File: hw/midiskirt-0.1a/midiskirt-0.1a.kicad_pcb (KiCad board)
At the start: 2 copper layers, 13 parts, among them J1 DIN-5, J2 DIN-5, J3 DIN-5, U1 MC6850, U2 C64-Exp-Port, U3 74LS30, U4 4049, U5 6N137

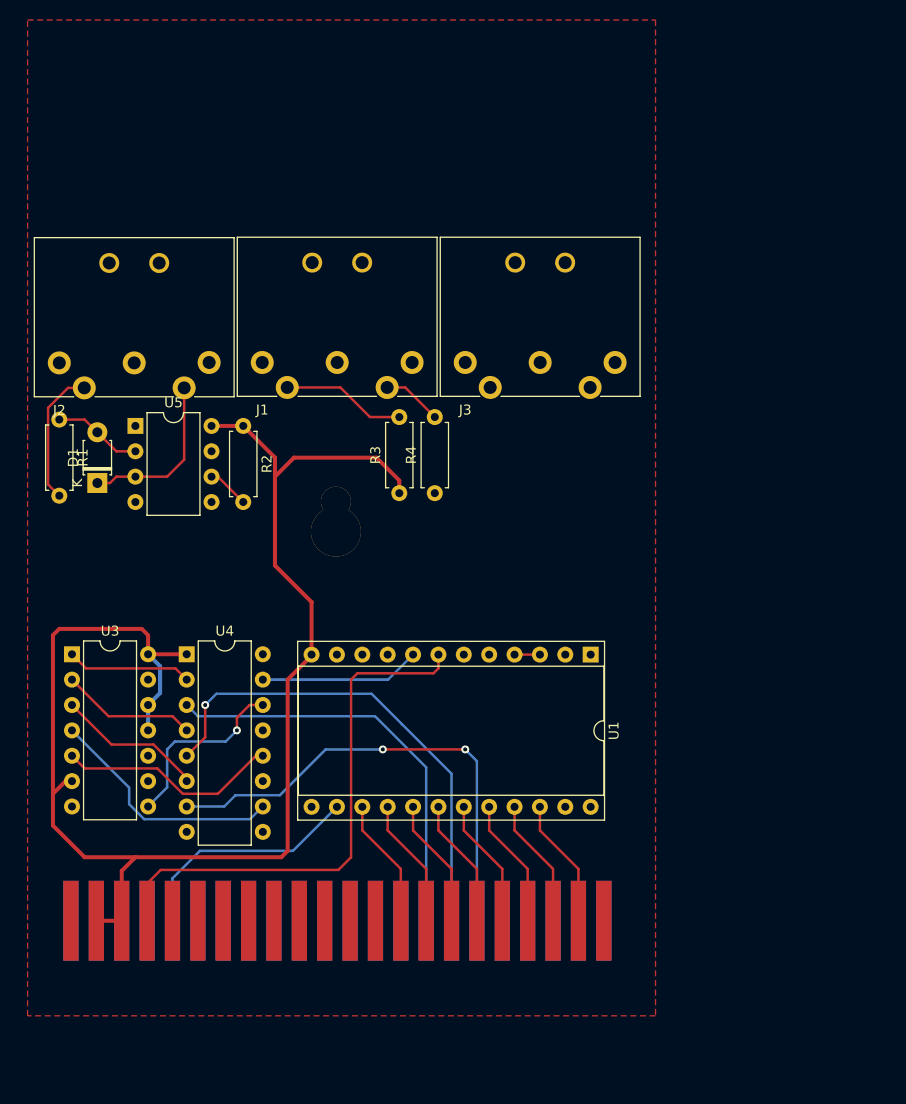
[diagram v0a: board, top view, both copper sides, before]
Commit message: probably bad, stuck version w discrete dip logic
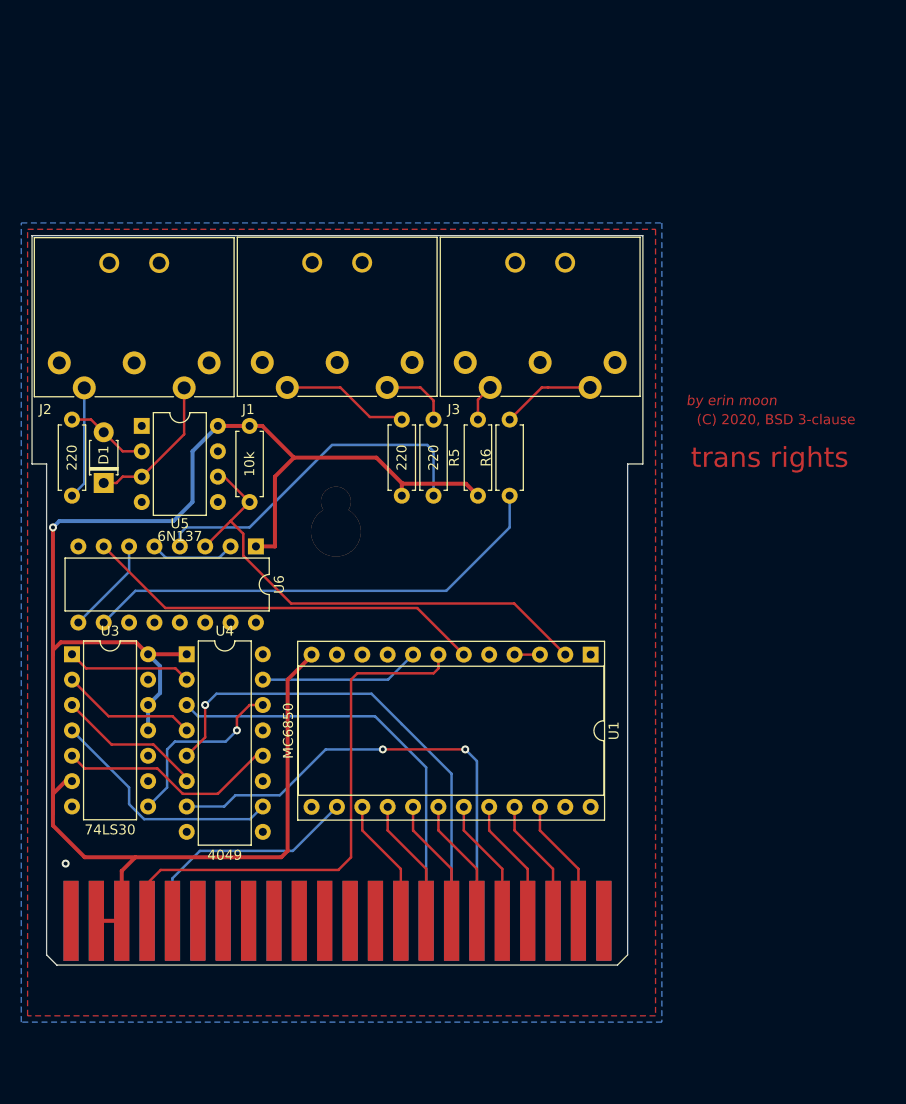
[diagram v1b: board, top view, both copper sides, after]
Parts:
- added R5: 220, Resistor_THT:R_Axial_DIN0207_L6.3mm_D2.5mm_P7.62mm_Horizontal, F.Cu at (132.7, 85.1)
- added R6: 220, Resistor_THT:R_Axial_DIN0207_L6.3mm_D2.5mm_P7.62mm_Horizontal, F.Cu at (135.9, 85.1)
- added U6: 4049, Package_DIP:DIP-16_W7.62mm, F.Cu at (110.5, 90.2)
- moved R1 1.27 mm to (92.1, 77.5)
- moved D1 0.64 mm to (95.2, 83.8)
- moved R2 0.64 mm to (109.9, 78.1)
- moved U5 0.64 mm to (99.1, 78.1)
- moved R3 0.36 mm to (125.1, 85.1)
- moved R4 0.28 mm to (128.3, 85.1)
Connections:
- net Net-(U2-PadX) renamed /a1
- J3 pad 2: Net-(J3-Pad2) -> GND
- R4 pad 1: Net-(R4-Pad1) -> (no net)
- U1 pad 10: /CS1 -> (no net)
- U1 pad 11: /RS -> (no net)
- U1 pad 13: /R~W~ -> (no net)
- U1 pad 2: /RxD -> (no net)
- U1 pad 5: Net-(U1-Pad5) -> (no net)
- U1 pad 6: /TxD -> (no net)
- U1 pad 8: /CS0 -> (no net)
- U1 pad 9: /~CS2~ -> (no net)
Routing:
- net (no net): track 0.00 -> 139.4 mm, vias 0 -> 1
- net /RxD: track 0.00 -> 50.8 mm
- net +5V: track 145.5 -> 178.1 mm, vias 0 -> 1
- net /CS0: track 16.1 -> 0.00 mm
- net Net-(U6-Pad6): track 0.00 -> 9.72 mm
- net Net-(J3-Pad5): track 0.00 -> 9.39 mm
- net Net-(U6-Pad2): track 0.00 -> 8.55 mm
- net /midi_in: track 4.23 -> 0.00 mm
- net Net-(J3-Pad4): track 0.00 -> 3.72 mm
- net Net-(J2-Pad4): track 13.7 -> 11.3 mm
- net Net-(D1-Pad1): track 16.8 -> 14.7 mm
- net Net-(J1-Pad5): track 6.00 -> 6.84 mm
- net Net-(D1-Pad2): track 8.94 -> 8.30 mm
- added copper zone on B.Cu, net GND
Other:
- board outline added: 61.2 x 73 mm
- board text added: "(C) 2020, BSD 3-clause"
- board text added: "by erin moon"
- board text added: "trans rights"

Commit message: smt updates
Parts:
- added U7: 4050, Package_SO:SOIC-16_4.55x10.3mm_P1.27mm, B.Cu at (95.9, 102.2)
- added U8: SN74LVC1404, Package_SO:SSOP-8_2.95x2.8mm_P0.65mm, F.Cu at (98.9, 113.0)
- added Y1: Crystal, Crystal:Crystal_HC49-U_Vertical, F.Cu at (92.7, 110.5)
- D1: footprint Diode_THT:D_T-1_P5.08mm_Horizontal -> Diode_SMD:D_SOD-123
- R1, R2: footprint Resistor_THT:R_Axial_DIN0207_L6.3mm_D2.5mm_P7.62mm_Horizontal -> Resistor_SMD:R_0603_1608Metric
- R3, R4, R5, R6: footprint Resistor_THT:R_Axial_DIN0207_L6.3mm_D2.5mm_P7.62mm_Horizontal -> Resistor_SMD:R_0603_1608Metric; moved to B.Cu
- U3: footprint Package_DIP:DIP-14_W7.62mm -> Package_SO:SOIC-14_3.9x8.7mm_P1.27mm; moved to B.Cu
- U4: value 4049 -> 74153; footprint Package_DIP:DIP-16_W7.62mm -> Package_SO:SOP-16_4.4x10.4mm_P1.27mm; moved to B.Cu
- U6: value 4049 -> 74157; footprint Package_DIP:DIP-16_W7.62mm -> Package_SO:SOP-16_4.4x10.4mm_P1.27mm; moved to B.Cu
- moved U4 38.3 mm to (140.0, 112.9), turned to 270 degrees
- moved U3 38.3 mm to (128.4, 113.0), turned to 90 degrees
- moved U6 23.7 mm to (116.8, 113.1), turned to 90 degrees
- moved R2 22.6 mm to (96.7, 96.5), turned to 180 degrees
- moved R4 13.5 mm to (120.0, 74.4), turned to 270 degrees
- moved R3 13.1 mm to (117.5, 74.4), turned to 270 degrees
- moved R5 11.8 mm to (137.8, 74.4), turned to 270 degrees
- moved R6 11.5 mm to (140.3, 74.4), turned to 270 degrees
- moved U5 8.47 mm to (101.0, 86.4), turned to 270 degrees
- moved R1 6.59 mm to (93.8, 83.8), turned to 180 degrees
- moved J1 6.35 mm to (111.1, 78.1)
- moved J3 6.35 mm to (131.4, 78.1)
- moved J2 6.35 mm to (90.8, 78.1)
- moved U1 4.48 mm to (144.8, 105.4)
- moved D1 2.80 mm to (98.0, 83.8), turned to 0 degrees
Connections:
- J1 pad 1: Net-(J1-Pad1) -> (no net)
- J1 pad 3: Net-(J1-Pad3) -> (no net)
- J2 pad 1: Net-(J2-Pad1) -> (no net)
- J2 pad 2: Net-(J2-Pad2) -> (no net)
- J2 pad 3: Net-(J2-Pad3) -> (no net)
- J3 pad 1: Net-(J3-Pad1) -> (no net)
- J3 pad 3: Net-(J3-Pad3) -> (no net)
- R4 pad 1: (no net) -> /midi_thru
- R6 pad 1: (no net) -> /midi_out
- U1 pad 13: (no net) -> /R~W~
- U1 pad 2: (no net) -> /RxD
- U1 pad 6: (no net) -> /TxD
- U2 pad 10: Net-(U2-Pad10) -> (no net)
- U2 pad 11: Net-(U2-Pad11) -> (no net)
- U2 pad 12: Net-(U2-Pad12) -> (no net)
- U2 pad 13: Net-(U2-Pad13) -> (no net)
- U2 pad 6: Net-(U2-Pad6) -> (no net)
- U2 pad 7: Net-(U2-Pad7) -> /~io1~
- U2 pad 8: Net-(U2-Pad8) -> (no net)
- U2 pad 9: Net-(U2-Pad9) -> (no net)
- U2 pad B: Net-(U2-PadB) -> (no net)
- U2 pad C: Net-(U2-PadC) -> (no net)
- U2 pad D: Net-(U2-PadD) -> (no net)
- U2 pad F: Net-(U2-PadF) -> (no net)
- U2 pad H: Net-(U2-PadH) -> (no net)
- U2 pad J: Net-(U2-PadJ) -> (no net)
- U2 pad K: Net-(U2-PadK) -> (no net)
- U2 pad L: Net-(U2-PadL) -> (no net)
- U2 pad M: Net-(U2-PadM) -> (no net)
- U2 pad N: Net-(U2-PadN) -> (no net)
- U2 pad P: Net-(U2-PadP) -> (no net)
- U2 pad R: Net-(U2-PadR) -> (no net)
- U2 pad V: Net-(U2-PadV) -> /a3
- U2 pad W: Net-(U2-PadW) -> /a2
- U2 pad Y: Net-(U2-PadY) -> (no net)
- U3 pad 1: Net-(U3-Pad1) -> /a4
- U3 pad 11: +5V -> GND
- U3 pad 12: +5V -> GND
- U3 pad 2: Net-(U3-Pad2) -> /a5
- U3 pad 3: Net-(U3-Pad3) -> /a6
- U3 pad 4: Net-(U3-Pad4) -> /~io1~
- U3 pad 6: +5V -> GND
- U3 pad 8: Net-(U3-Pad8) -> /cs1
- U4 pad 1: +5V -> GND
- U4 pad 10: Net-(U3-Pad4) -> /a1
- U4 pad 11: /asel0 -> GND
- U4 pad 12: Net-(U3-Pad5) -> /a2
- U4 pad 13: (no net) -> GND
- U4 pad 14: Net-(U3-Pad8) -> /sel_a
- U4 pad 15: /CS0 -> GND
- U4 pad 16: (no net) -> +5V
- U4 pad 2: Net-(U3-Pad1) -> (no net)
- U4 pad 3: /a6 -> /a2
- U4 pad 4: Net-(U3-Pad2) -> (no net)
- U4 pad 5: /a5 -> GND
- U4 pad 6: Net-(U3-Pad3) -> /a3
- U4 pad 7: /a4 -> /cs1
- U4 pad 9: /~io1~ -> (no net)
- U5 pad 1: Net-(U5-Pad1) -> (no net)
- U5 pad 7: Net-(U5-Pad7) -> (no net)
- U6 pad 1: +5V -> /sel_a
- U6 pad 10: /midi_out -> (no net)
- U6 pad 15: (no net) -> GND
- U6 pad 16: (no net) -> +5V
- U6 pad 2: Net-(U6-Pad2) -> /a2
- U6 pad 3: /RxD -> /a3
- U6 pad 4: /midi_thru -> Net-(U3-Pad5)
- U6 pad 5: Net-(U6-Pad2) -> /cart-r~w~
- U6 pad 6: Net-(U6-Pad6) -> /a1
- U6 pad 7: /TxD -> /R~W~
- U6 pad 9: Net-(U6-Pad6) -> (no net)
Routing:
- net (no net): track 139.4 -> 0.00 mm, vias 1 -> 0
- net /midi_out: track 0.00 -> 72.0 mm
- net /midi_thru: track 0.00 -> 44.8 mm
- net /TxD: track 0.00 -> 42.7 mm
- net /a1: track 0.00 -> 42.4 mm, vias 0 -> 2
- net /a3: track 0.00 -> 41.7 mm, vias 0 -> 3
- net /a2: track 0.00 -> 40.1 mm
- net /a5: track 49.0 -> 12.6 mm, vias 1 -> 0
- net /a4: track 47.9 -> 12.9 mm, vias 2 -> 0
- net /~io1~: track 0.00 -> 31.4 mm, vias 0 -> 1
- net +5V: track 178.1 -> 149.1 mm, vias 1 -> 7
- net /a6: track 41.9 -> 13.1 mm
- net Net-(U3-Pad4): track 24.3 -> 0.00 mm
- net /cart-r~w~: track 0.00 -> 22.9 mm, vias 0 -> 1
- net GND: track 0.00 -> 21.7 mm, vias 0 -> 4
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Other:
- board size 61.2 x 73 mm -> 61.2 x 66.7 mm
- board text added: "midiskirt 0.1a"

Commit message: first design that seems orderable
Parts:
- removed the R3 at (117.5, 74.4)
- removed the R4 at (120.0, 74.4)
- removed the U6 at (116.8, 113.1)
- added C1: 0.1u, Capacitor_SMD:C_0603_1608Metric, F.Cu at (101.0, 96.5)
- added C2: 0.1u, Capacitor_SMD:C_0603_1608Metric, F.Cu at (98.9, 107.8)
- added C3: 0.1u, Capacitor_SMD:C_0603_1608Metric, F.Cu at (111.8, 90.2)
- added C4: 0.1u, Capacitor_SMD:C_0603_1608Metric, B.Cu at (113.2, 114.9)
- added C5: 0.1u, Capacitor_SMD:C_0603_1608Metric, B.Cu at (136.4, 118.1)
- added C6: 0.1u, Capacitor_SMD:C_0603_1608Metric, B.Cu at (131.4, 108.5)
- added C7: 0.1u, Capacitor_SMD:C_0603_1608Metric, F.Cu at (119.1, 102.9)
- added R1: 220, Resistor_SMD:R_0603_1608Metric, B.Cu at (117.5, 74.4)
- added R6: 10k, Resistor_SMD:R_0603_1608Metric, F.Cu at (97.2, 96.5)
- added SW1: SW_DP3T, midiskirt:C&K_JS203011CQN, F.Cu at (118.6, 99.1)
- added U2: 74LS393, Package_SO:SO-14_5.3x10.2mm_P1.27mm, B.Cu at (99.7, 104.1)
- added U5: 74153, Package_SO:SOP-16_4.4x10.4mm_P1.27mm, B.Cu at (140.0, 112.9)
- R2: value 10k -> 220; moved to B.Cu
- U1: value MC6850 -> 74LS30; footprint Package_DIP:DIP-24_W15.24mm_Socket -> Package_SO:SOIC-14_3.9x8.7mm_P1.27mm; moved to B.Cu
- U3: value 74LS30 -> 74LVC3G16; footprint Package_SO:SOIC-14_3.9x8.7mm_P1.27mm -> Package_SO:TSSOP-8_3x3mm_P0.65mm; moved to F.Cu
- U4: value 74153 -> MC6850; footprint Package_SO:SOP-16_4.4x10.4mm_P1.27mm -> Package_DIP:DIP-24_W15.24mm_Socket; moved to F.Cu
- U7: value 4050 -> SN74LVC1GX04; footprint Package_SO:SOIC-16_4.55x10.3mm_P1.27mm -> Package_TO_SOT_SMD:SOT-23-6_Handsoldering; moved to F.Cu
- U8: value SN74LVC1404 -> SN74LV4053A; footprint Package_SO:SSOP-8_2.95x2.8mm_P0.65mm -> Package_SO:SOIC-16_3.9x9.9mm_P1.27mm; moved to B.Cu
- Y1: value Crystal -> 2 MHz; footprint Crystal:Crystal_HC49-U_Vertical -> Crystal:Crystal_HC49-4H_Vertical
- moved R2 32.1 mm to (120.0, 74.4), turned to 270 degrees
- moved U3 30.0 mm to (108.9, 90.2), turned to 270 degrees
- moved U1 18.0 mm to (128.4, 113.0), turned to 90 degrees
- moved U8 11.8 mm to (109.8, 108.6)
- moved U4 8.93 mm to (144.8, 105.4)
- moved Y1 8.91 mm to (93.3, 101.6)
- moved U7 4.29 mm to (99.7, 104.1)
- moved J3 0.41 mm to (131.9, 78.1)
- moved J2 0.36 mm to (90.5, 78.1)
- renumbered R1 to R3, R5 to R4, R6 to R5, U2 to U6, U5 to U9
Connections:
- R2 pad 1: +5V -> /midi_thru
- R2 pad 2: /midi_in -> Net-(J1-Pad5)
- U1 pad 1: GND -> /a4
- U1 pad 11: (no net) -> GND
- U1 pad 12: +5V -> GND
- U1 pad 13: /R~W~ -> (no net)
- U1 pad 14: /phi2 -> +5V
- U1 pad 2: /RxD -> /a5
- U1 pad 3: /6850_CLK -> /a6
- U1 pad 4: /6850_CLK -> /~io1~
- U1 pad 5: (no net) -> Net-(U1-Pad5)
- U1 pad 6: /TxD -> GND
- U1 pad 7: /~irq~ -> GND
- U1 pad 8: (no net) -> /cs1
- U3 pad 1: /a4 -> /midi_in
- U3 pad 2: /a5 -> /midi_out
- U3 pad 3: /a6 -> /midi_in
- U3 pad 4: /~io1~ -> GND
- U3 pad 5: Net-(U3-Pad5) -> /midi_thru
- U3 pad 6: GND -> /TxD
- U3 pad 7: GND -> /RxD
- U3 pad 8: /cs1 -> +5V
- U4 pad 10: /a1 -> (no net)
- U4 pad 11: GND -> (no net)
- U4 pad 12: /a2 -> +5V
- U4 pad 13: GND -> /R~W~
- U4 pad 14: /sel_a -> /phi2
- U4 pad 15: GND -> /d7
- U4 pad 16: +5V -> /d6
- U4 pad 2: (no net) -> /RxD
- U4 pad 3: /a2 -> /6850_CLK
- U4 pad 4: (no net) -> /6850_CLK
- U4 pad 5: GND -> (no net)
- U4 pad 6: /a3 -> /TxD
- U4 pad 7: /cs1 -> /~irq~
- U4 pad 8: GND -> (no net)
- U7 pad 1: +5V -> (no net)
- U7 pad 2: /midi_out -> GND
- U7 pad 3: /TxD -> Net-(U7-Pad3)
- U7 pad 4: /midi_thru -> Net-(U7-Pad4)
- U7 pad 5: /midi_in -> +5V
- U7 pad 6: /RxD -> /2mhz
- U8 pad 1: (no net) -> /2mhz
- U8 pad 2: Net-(U8-Pad2) -> /500khz
- U8 pad 3: Net-(U8-Pad3) -> /a1
- U8 pad 4: GND -> /R~W~
- U8 pad 5: (no net) -> /cart-r~w~
- U8 pad 6: (no net) -> GND
- U8 pad 7: (no net) -> GND
- U8 pad 8: +5V -> GND
- Y1 pad 1: Net-(U8-Pad2) -> Net-(U7-Pad3)
- Y1 pad 2: Net-(U8-Pad3) -> Net-(U7-Pad4)
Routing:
- net +5V: track 149.1 -> 204.4 mm, vias 7 -> 8
- net /sel_b: track 0.00 -> 38.4 mm, vias 0 -> 1
- net /sel_a: track 18.9 -> 56.9 mm, vias 0 -> 3
- net /6850_CLK: track 2.54 -> 30.1 mm, vias 0 -> 1
- net /midi_out: track 72.0 -> 46.0 mm, vias 0 -> 1
- net /2mhz: track 0.00 -> 19.1 mm, vias 0 -> 2
- net Net-(U1-Pad5): track 0.00 -> 17.5 mm
- net /cart-r~w~: track 22.9 -> 38.8 mm
- net /a1: track 42.4 -> 56.3 mm, vias 2 -> 0
- net Net-(U3-Pad5): track 12.2 -> 0.00 mm
- net /midi_thru: track 44.8 -> 32.6 mm, vias 0 -> 1
- net /R~W~: track 5.76 -> 17.5 mm
- net /midi_in: track 9.60 -> 20.6 mm, vias 1 -> 0
- net /500khz: track 0.00 -> 10.5 mm
- net /a3: track 41.7 -> 52.1 mm, vias 3 -> 2
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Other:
- board size 61.2 x 66.7 mm -> 61.8 x 66.7 mm
- board text added: "Blahaj Inside. may be used to make bangers. function not guaranteed when operated by cis people."
- board text added: "C1-7: .1uF 0608"
- board text added: "JLCJLCJLCJLC"
